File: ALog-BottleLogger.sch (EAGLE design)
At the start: 102 parts, among them IC2 ATMEGA644M, Q1 220mA/50V/3.5Ω, Q11 220mA/50V/3.5Ω, Q12 4.3A/20V/54mΩ, Q5 4.3A/20V/54mΩ, Q6 4.3A/20V/54mΩ, Q7 4.3A/20V/54mΩ, Q8 220mA/50V/3.5Ω, Q9 220mA/50V/3.5Ω, U2 FT231X-Q

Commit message: Changed cap sizes on 10 and 22 uF to 805 and fixed MISO/MOSI labels on SD card.
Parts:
- C1, C10, C2, C22, C24, C25: device rcl:C-EUC0603 -> rcl:C-EUC0805
- C12, C13, C14, C15, C16, C17, C28, C29, C30, C31, C32, C33, C34, C35: value 10nF -> 0.1uF
- C23: value 10pF -> 33pF
- U$6: value TPS63061 -> TPS63060
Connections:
- removed net D21: IC2.(PCINT21/TDI)PC5
- removed net MISO/D5: SD.DATA_OUT
- removed net MOSI/D6: SD.DATA_IN
- net MISO/D6: now also SD.DATA_OUT
- net MOSI/D5: now also SD.DATA_IN
- net SD_CS: now also IC2.(PCINT21/TDI)PC5
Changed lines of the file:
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@@
 <part name="GND30" library="supply1" deviceset="GND" device=""/>
 <part name="GND31" library="supply1" deviceset="GND" device=""/>
-<part name="C12" library="rcl" deviceset="C-EU" device="C0603" value="10nF"/>
-<part name="C13" library="rcl" deviceset="C-EU" device="C0603" value="10nF"/>
-<part name="C14" library="rcl" deviceset="C-EU" device="C0603" value="10nF"/>
-<part name="C15" library="rcl" deviceset="C-EU" device="C0603" value="10nF"/>
-<part name="C16" library="rcl" deviceset="C-EU" device="C0603" value="10nF"/>
-<part name="C17" library="rcl" deviceset="C-EU" device="C0603" value="10nF"/>
+<part name="C12" library="rcl" deviceset="C-EU" device="C0603" value="0.1uF"/>
+<part name="C13" library="rcl" deviceset="C-EU" device="C0603" value="0.1uF"/>
+<part name="C14" library="rcl" deviceset="C-EU" device="C0603" value="0.1uF"/>
+<part name="C15" library="rcl" deviceset="C-EU" device="C0603" value="0.1uF"/>
+<part name="C16" library="rcl" deviceset="C-EU" device="C0603" value="0.1uF"/>
+<part name="C17" library="rcl" deviceset="C-EU" device="C0603" value="0.1uF"/>
 <part name="J8" library="SparkFun-Connectors" deviceset="CONN_10" device=""/>
 <part name="ISP2" library="adafruit" deviceset="AVRISP" device="-6"/>
@@
 <part name="J1" library="SparkFun-Connectors" deviceset="CONN_10" device=""/>
 <part name="J2" library="SparkFun-Connectors" deviceset="CONN_10" device=""/>
-<part name="U$6" library="Custom" deviceset="TPS306X" device="" value="TPS63061"/>
+<part name="U$6" library="Custom" deviceset="TPS306X" device="" value="TPS63060"/>
 <part name="U$9" library="Custom" deviceset="WE-MAIA(INDUCTOR)" device="" value="1uH"/>
 <part name="C21" library="rcl" deviceset="C-EU" device="C0603" value="0.1uF"/>
-<part name="C22" library="rcl" deviceset="C-EU" device="C0603" value="10uF"/>
+<part name="C22" library="rcl" deviceset="C-EU" device="C0805" value="10uF"/>
 <part name="GND38" library="SparkFun-PowerSymbols" deviceset="GND" device=""/>
-<part name="C23" library="rcl" deviceset="C-EU" device="C0603" value="10pF"/>
-<part name="C24" library="rcl" deviceset="C-EU" device="C0603" value="22uF"/>
+<part name="C23" library="rcl" deviceset="C-EU" device="C0603" value="33pF"/>
+<part name="C24" library="rcl" deviceset="C-EU" device="C0805" value="22uF"/>
 <part name="GND39" library="SparkFun-PowerSymbols" deviceset="GND" device=""/>
 <part name="GND40" library="SparkFun-PowerSymbols" deviceset="GND" device=""/>
-<part name="C25" library="rcl" deviceset="C-EU" device="C0603" value="10uF"/>
+<part name="C25" library="rcl" deviceset="C-EU" device="C0805" value="10uF"/>
 <part name="R15" library="rcl" deviceset="R-EU_" device="R0603" value="143k"/>
 <part name="R16" library="rcl" deviceset="R-EU_" device="R0603" value="953k"/>
-<part name="C1" library="rcl" deviceset="C-EU" device="C0603" value="22uF"/>
-<part name="C2" library="rcl" deviceset="C-EU" device="C0603" value="22uF"/>
+<part name="C1" library="rcl" deviceset="C-EU" device="C0805" value="22uF"/>
+<part name="C2" library="rcl" deviceset="C-EU" device="C0805" value="22uF"/>
 <part name="U$3" library="texas" deviceset="TPS6217X" device=""/>
 <part name="GND2" library="supply1" deviceset="GND" device=""/>
@@
 <part name="L1" library="Custom" deviceset="WE-LSQ(INDUCTOR)" device="" value="10uH"/>
 <part name="GND16" library="supply1" deviceset="GND" device=""/>
-<part name="C10" library="rcl" deviceset="C-EU" device="C0603" value="22uF"/>
+<part name="C10" library="rcl" deviceset="C-EU" device="C0805" value="22uF"/>
 <part name="R1" library="rcl" deviceset="R-EU_" device="R0603" value="10k"/>
 <part name="U$4" library="Custom" deviceset="SKRPABE010" device=""/>
@@
 <part name="R17" library="rcl" deviceset="R-EU_" device="R0603" value="10k"/>
 <part name="GND1" library="supply1" deviceset="GND" device=""/>
-<part name="C28" library="rcl" deviceset="C-EU" device="C0603" value="10nF"/>
+<part name="C28" library="rcl" deviceset="C-EU" device="C0603" value="0.1uF"/>
 <part name="R23" library="rcl" deviceset="R-EU_" device="R0603" value="10k"/>
 <part name="GND19" library="supply1" deviceset="GND" device=""/>
-<part name="C29" library="rcl" deviceset="C-EU" device="C0603" value="10nF"/>
+<part name="C29" library="rcl" deviceset="C-EU" device="C0603" value="0.1uF"/>
 <part name="R24" library="rcl" deviceset="R-EU_" device="R0603" value="10k"/>
 <part name="SJ1" library="SparkFun-Retired" deviceset="SOLDERJUMPER-OLD" device="TRACE"/>
@@
 <part name="GND37" library="supply1" deviceset="GND" device=""/>
 <part name="GND41" library="supply1" deviceset="GND" device=""/>
-<part name="C30" library="rcl" deviceset="C-EU" device="C0603" value="10nF"/>
-<part name="C31" library="rcl" deviceset="C-EU" device="C0603" value="10nF"/>
+<part name="C30" library="rcl" deviceset="C-EU" device="C0603" value="0.1uF"/>
+<part name="C31" library="rcl" deviceset="C-EU" device="C0603" value="0.1uF"/>
 <part name="GND42" library="supply1" deviceset="GND" device=""/>
-<part name="C32" library="rcl" deviceset="C-EU" device="C0603" value="10nF"/>
+<part name="C32" library="rcl" deviceset="C-EU" device="C0603" value="0.1uF"/>
 <part name="GND43" library="supply1" deviceset="GND" device=""/>
-<part name="C33" library="rcl" deviceset="C-EU" device="C0603" value="10nF"/>
+<part name="C33" library="rcl" deviceset="C-EU" device="C0603" value="0.1uF"/>
 <part name="GND44" library="supply1" deviceset="GND" device=""/>
 <part name="GND45" library="supply1" deviceset="GND" device=""/>
-<part name="C34" library="rcl" deviceset="C-EU" device="C0603" value="10nF"/>
-<part name="C35" library="rcl" deviceset="C-EU" device="C0603" value="10nF"/>
+<part name="C34" library="rcl" deviceset="C-EU" device="C0603" value="0.1uF"/>
+<part name="C35" library="rcl" deviceset="C-EU" device="C0603" value="0.1uF"/>
 <part name="LED1" library="SparkFun-LED" deviceset="LED" device="0603" value="Yellow"/>
 <part name="LED2" library="SparkFun-LED" deviceset="LED" device="0603" value="Blue"/>
@@
 </segment>
 </net>
-<net name="MOSI/D6" class="0">
-<segment>
-<wire x1="335.28" y1="5.08" x2="340.36" y2="5.08" width="0.1524" layer="91"/>
-<label x="337.82" y="5.08" size="1.778" layer="95"/>
-<pinref part="SD" gate="G$1" pin="DATA_IN"/>
-</segment>
-</net>
-<net name="MISO/D5" class="0">
-<segment>
-<wire x1="335.28" y1="2.54" x2="340.36" y2="2.54" width="0.1524" layer="91"/>
-<label x="337.82" y="2.54" size="1.778" layer="95"/>
-<pinref part="SD" gate="G$1" pin="DATA_OUT"/>
-</segment>
-</net>
 <net name="GND" class="0">
 <segment>
@@
 <pinref part="SD" gate="G$1" pin="CS"/>
 </segment>
+<segment>
+<pinref part="IC2" gate="G$1" pin="(PCINT21/TDI)PC5"/>
+<wire x1="241.3" y1="2.54" x2="248.92" y2="2.54" width="0.1524" layer="91"/>
+<label x="243.84" y="2.54" size="1.778" layer="95"/>
+</segment>
 </net>
 <net name="SD_VCC" class="0">
@@
 <wire x1="241.3" y1="-25.4" x2="248.92" y2="-25.4" width="0.1524" layer="91"/>
 <label x="243.84" y="-25.4" size="1.778" layer="95"/>
-</segment>
-</net>
-<net name="D21" class="0">
-<segment>
-<pinref part="IC2" gate="G$1" pin="(PCINT21/TDI)PC5"/>
-<wire x1="241.3" y1="2.54" x2="248.92" y2="2.54" width="0.1524" layer="91"/>
-<label x="243.84" y="2.54" size="1.778" layer="95"/>
 </segment>
 </net>
@@
 <label x="243.84" y="25.4" size="1.778" layer="95"/>
 </segment>
+<segment>
+<wire x1="335.28" y1="5.08" x2="340.36" y2="5.08" width="0.1524" layer="91"/>
+<label x="337.82" y="5.08" size="1.778" layer="95"/>
+<pinref part="SD" gate="G$1" pin="DATA_IN"/>
+</segment>
 </net>
 <net name="MISO/D6" class="0">
@@
 <label x="243.84" y="27.94" size="1.778" layer="95"/>
 </segment>
-</net>
+<segment>
+<wire x1="335.28" y1="2.54" x2="340.36" y2="2.54" width="0.1524" layer="91"/>
+<label x="337.82" y="2.54" size="1.778" layer="95"/>
+<pinref part="SD" gate="G$1" pin="DATA_OUT"/>
+</segment>
+</net>

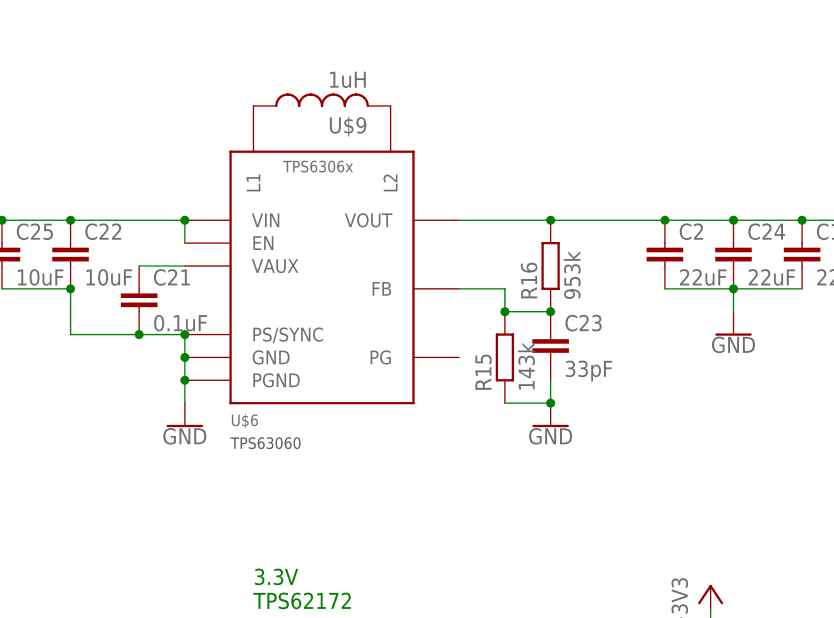
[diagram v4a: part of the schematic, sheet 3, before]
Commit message: Corrected footprint of 5V regulator
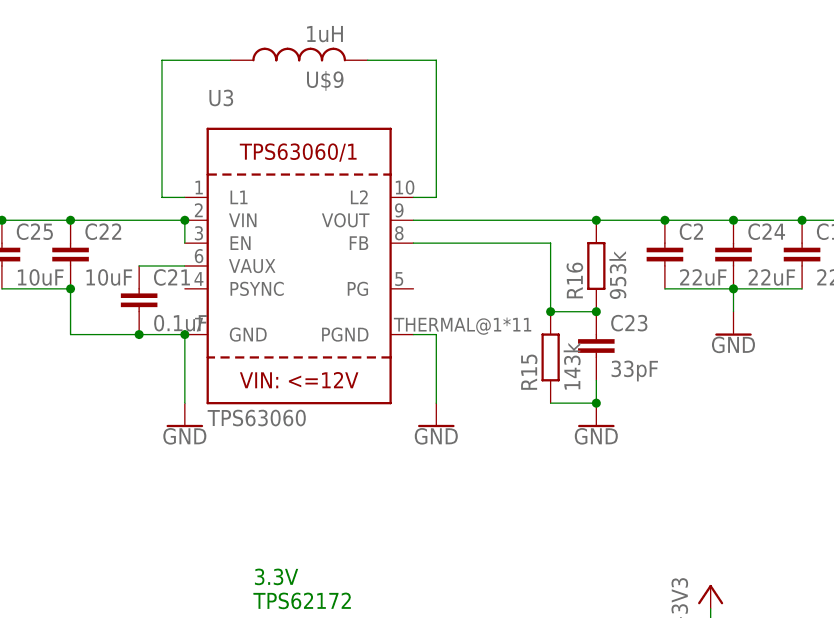
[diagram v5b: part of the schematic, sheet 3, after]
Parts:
- removed U$6: TPS63060, Custom:TPS306X
- added U3: TPS63060, microbuilder:VREG_TPS63060/1
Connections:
- removed net N$19: U$6.L2, U$9.2
- removed net N$20: U$6.L1, U$9.1
- new net N$27: U$9.1, U3.L1
- new net N$32: U$9.2, U3.L2
- net +5V: now also U3.VOUT; no longer U$6.VOUT
- net BATT+: now also U3.EN, U3.VIN; no longer U$6.EN, U$6.VIN
- net GND: now also U3.GND, U3.PGND; no longer U$6.GND, U$6.PGND, U$6.PS/SYNC
- net N$21: now also U3.VAUX; no longer U$6.VAUX
- net N$22: now also U3.FB; no longer U$6.FB
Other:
- moved on the sheet: C23, R15, R16, U$9
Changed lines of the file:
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@@
 <part name="J1" library="SparkFun-Connectors" deviceset="CONN_10" device=""/>
 <part name="J2" library="SparkFun-Connectors" deviceset="CONN_10" device=""/>
-<part name="U$6" library="Custom" deviceset="TPS306X" device="" value="TPS63060"/>
 <part name="U$9" library="Custom" deviceset="WE-MAIA(INDUCTOR)" device="" value="1uH"/>
 <part name="C21" library="rcl" deviceset="C-EU" device="C0603" value="0.1uF"/>
@@
 <part name="GND21" library="supply1" deviceset="GND" device=""/>
 <part name="P+5" library="supply1" deviceset="+5V" device=""/>
+<part name="U3" library="microbuilder" deviceset="VREG_TPS63060/1" device="" value="TPS63060"/>
+<part name="GND33" library="SparkFun-PowerSymbols" deviceset="GND" device=""/>
 </parts>
 <sheets>
@@
 </plain>
 <instances>
-<instance part="U$6" gate="G$1" x="-63.5" y="101.6"/>
-<instance part="U$9" gate="G$1" x="-63.5" y="119.38" rot="R90"/>
+<instance part="U$9" gate="G$1" x="-66.04" y="124.46" rot="R90"/>
 <instance part="C21" gate="G$1" x="-83.82" y="99.06"/>
 <instance part="C22" gate="G$1" x="-91.44" y="104.14"/>
 <instance part="GND38" gate="1" x="-78.74" y="83.82"/>
-<instance part="C23" gate="G$1" x="-38.1" y="93.98"/>
+<instance part="C23" gate="G$1" x="-33.02" y="93.98"/>
 <instance part="C24" gate="G$1" x="-17.78" y="104.14"/>
-<instance part="GND39" gate="1" x="-38.1" y="83.82"/>
+<instance part="GND39" gate="1" x="-33.02" y="83.82"/>
 <instance part="GND40" gate="1" x="-17.78" y="93.98"/>
 <instance part="C25" gate="G$1" x="-99.06" y="104.14"/>
-<instance part="R15" gate="G$1" x="-43.18" y="91.44" rot="R90"/>
-<instance part="R16" gate="G$1" x="-38.1" y="101.6" rot="R90"/>
+<instance part="R15" gate="G$1" x="-38.1" y="91.44" rot="R90"/>
+<instance part="R16" gate="G$1" x="-33.02" y="101.6" rot="R90"/>
 <instance part="C1" gate="G$1" x="-10.16" y="104.14"/>
 <instance part="C2" gate="G$1" x="-25.4" y="104.14"/>
@@
 <instance part="C6" gate="G$1" x="-27.94" y="10.16"/>
 <instance part="GND7" gate="1" x="-27.94" y="0"/>
+<instance part="U3" gate="G$1" x="-66.04" y="101.6"/>
+<instance part="GND33" gate="1" x="-50.8" y="83.82"/>
 </instances>
 <busses>
@@
 <net name="GND" class="0">
 <segment>
-<pinref part="U$6" gate="G$1" pin="PS/SYNC"/>
 <pinref part="C21" gate="G$1" pin="2"/>
 <wire x1="-78.74" y1="93.98" x2="-83.82" y2="93.98" width="0.1524" layer="91"/>
@@
 <wire x1="-91.44" y1="93.98" x2="-83.82" y2="93.98" width="0.1524" layer="91"/>
 <junction x="-83.82" y="93.98"/>
-<pinref part="U$6" gate="G$1" pin="PGND"/>
-<pinref part="U$6" gate="G$1" pin="GND"/>
-<wire x1="-78.74" y1="88.9" x2="-78.74" y2="91.44" width="0.1524" layer="91"/>
-<wire x1="-78.74" y1="93.98" x2="-78.74" y2="91.44" width="0.1524" layer="91"/>
-<junction x="-78.74" y="93.98"/>
-<junction x="-78.74" y="91.44"/>
+<wire x1="-78.74" y1="93.98" x2="-78.74" y2="86.36" width="0.1524" layer="91"/>
 <pinref part="GND38" gate="1" pin="GND"/>
-<wire x1="-78.74" y1="86.36" x2="-78.74" y2="88.9" width="0.1524" layer="91"/>
-<junction x="-78.74" y="88.9"/>
 <pinref part="C25" gate="G$1" pin="2"/>
 <wire x1="-99.06" y1="99.06" x2="-91.44" y2="99.06" width="0.1524" layer="91"/>
 <junction x="-91.44" y="99.06"/>
+<pinref part="U3" gate="G$1" pin="GND"/>
+<junction x="-78.74" y="93.98"/>
 </segment>
 <segment>
 <pinref part="GND39" gate="1" pin="GND"/>
 <pinref part="C23" gate="G$1" pin="2"/>
-<wire x1="-38.1" y1="86.36" x2="-38.1" y2="88.9" width="0.1524" layer="91"/>
+<wire x1="-33.02" y1="86.36" x2="-33.02" y2="88.9" width="0.1524" layer="91"/>
 <pinref part="R15" gate="G$1" pin="1"/>
-<wire x1="-43.18" y1="86.36" x2="-38.1" y2="86.36" width="0.1524" layer="91"/>
-<junction x="-38.1" y="86.36"/>
+<wire x1="-38.1" y1="86.36" x2="-33.02" y2="86.36" width="0.1524" layer="91"/>
+<junction x="-33.02" y="86.36"/>
 </segment>
 <segment>
@@
 <pinref part="C6" gate="G$1" pin="2"/>
 </segment>
+<segment>
+<pinref part="U3" gate="G$1" pin="PGND"/>
+<pinref part="GND33" gate="1" pin="GND"/>
+<wire x1="-53.34" y1="93.98" x2="-50.8" y2="93.98" width="0.1524" layer="91"/>
+<wire x1="-50.8" y1="93.98" x2="-50.8" y2="86.36" width="0.1524" layer="91"/>
+</segment>
 </net>
 <net name="BATT+" class="0">
 <segment>
-<pinref part="U$6" gate="G$1" pin="VIN"/>
-<pinref part="U$6" gate="G$1" pin="EN"/>
 <wire x1="-78.74" y1="104.14" x2="-78.74" y2="106.68" width="0.1524" layer="91"/>
-<junction x="-78.74" y="106.68"/>
 <pinref part="C22" gate="G$1" pin="1"/>
 <wire x1="-91.44" y1="106.68" x2="-78.74" y2="106.68" width="0.1524" layer="91"/>
@@
 <junction x="-99.06" y="106.68"/>
 <label x="-106.68" y="106.68" size="1.778" layer="95"/>
-</segment>
-</net>
-<net name="N$19" class="0">
-<segment>
-<pinref part="U$6" gate="G$1" pin="L2"/>
-<pinref part="U$9" gate="G$1" pin="2"/>
-</segment>
-</net>
-<net name="N$20" class="0">
-<segment>
-<pinref part="U$6" gate="G$1" pin="L1"/>
-<pinref part="U$9" gate="G$1" pin="1"/>
+<pinref part="U3" gate="G$1" pin="VIN"/>
+<junction x="-78.74" y="106.68"/>
+<pinref part="U3" gate="G$1" pin="EN"/>
 </segment>
 </net>
 <net name="N$21" class="0">
 <segment>
-<pinref part="U$6" gate="G$1" pin="VAUX"/>
 <pinref part="C21" gate="G$1" pin="1"/>
 <wire x1="-78.74" y1="101.6" x2="-83.82" y2="101.6" width="0.1524" layer="91"/>
+<pinref part="U3" gate="G$1" pin="VAUX"/>
 </segment>
 </net>
@@
 <pinref part="C23" gate="G$1" pin="1"/>
 <pinref part="R15" gate="G$1" pin="2"/>
-<wire x1="-43.18" y1="96.52" x2="-38.1" y2="96.52" width="0.1524" layer="91"/>
-<pinref part="U$6" gate="G$1" pin="FB"/>
-<wire x1="-48.26" y1="99.06" x2="-43.18" y2="99.06" width="0.1524" layer="91"/>
-<wire x1="-43.18" y1="99.06" x2="-43.18" y2="96.52" width="0.1524" layer="91"/>
-<junction x="-43.18" y="96.52"/>
+<wire x1="-38.1" y1="96.52" x2="-33.02" y2="96.52" width="0.1524" layer="91"/>
+<junction x="-38.1" y="96.52"/>
 <pinref part="R16" gate="G$1" pin="1"/>
-<junction x="-38.1" y="96.52"/>
+<junction x="-33.02" y="96.52"/>
+<pinref part="U3" gate="G$1" pin="FB"/>
+<wire x1="-53.34" y1="104.14" x2="-38.1" y2="104.14" width="0.1524" layer="91"/>
+<wire x1="-38.1" y1="104.14" x2="-38.1" y2="96.52" width="0.1524" layer="91"/>
 </segment>
 </net>
@@
 <pinref part="C24" gate="G$1" pin="1"/>
 <junction x="-17.78" y="106.68"/>
-<pinref part="U$6" gate="G$1" pin="VOUT"/>
-<wire x1="-48.26" y1="106.68" x2="-38.1" y2="106.68" width="0.1524" layer="91"/>
-<wire x1="-38.1" y1="106.68" x2="-25.4" y2="106.68" width="0.1524" layer="91"/>
+<wire x1="-53.34" y1="106.68" x2="-33.02" y2="106.68" width="0.1524" layer="91"/>
+<wire x1="-33.02" y1="106.68" x2="-25.4" y2="106.68" width="0.1524" layer="91"/>
 <wire x1="-25.4" y1="106.68" x2="-17.78" y2="106.68" width="0.1524" layer="91"/>
 <wire x1="-17.78" y1="106.68" x2="-10.16" y2="106.68" width="0.1524" layer="91"/>
 <pinref part="R16" gate="G$1" pin="2"/>
-<junction x="-38.1" y="106.68"/>
+<junction x="-33.02" y="106.68"/>
 <pinref part="C1" gate="G$1" pin="1"/>
 <wire x1="-10.16" y1="106.68" x2="0" y2="106.68" width="0.1524" layer="91"/>
@@
 <pinref part="P+2" gate="1" pin="+5V"/>
 <wire x1="0" y1="106.68" x2="0" y2="109.22" width="0.1524" layer="91"/>
+<pinref part="U3" gate="G$1" pin="VOUT"/>
 </segment>
 <segment>
@@
 </segment>
 </net>
+<net name="N$27" class="0">
+<segment>
+<pinref part="U3" gate="G$1" pin="L1"/>
+<wire x1="-78.74" y1="109.22" x2="-81.28" y2="109.22" width="0.1524" layer="91"/>
+<wire x1="-81.28" y1="109.22" x2="-81.28" y2="124.46" width="0.1524" layer="91"/>
+<pinref part="U$9" gate="G$1" pin="1"/>
+<wire x1="-81.28" y1="124.46" x2="-73.66" y2="124.46" width="0.1524" layer="91"/>
+</segment>
+</net>
+<net name="N$32" class="0">
+<segment>
+<pinref part="U$9" gate="G$1" pin="2"/>
+<wire x1="-58.42" y1="124.46" x2="-50.8" y2="124.46" width="0.1524" layer="91"/>
+<wire x1="-50.8" y1="124.46" x2="-50.8" y2="109.22" width="0.1524" layer="91"/>
+<pinref part="U3" gate="G$1" pin="L2"/>
+<wire x1="-50.8" y1="109.22" x2="-53.34" y2="109.22" width="0.1524" layer="91"/>
+</segment>
+</net>
